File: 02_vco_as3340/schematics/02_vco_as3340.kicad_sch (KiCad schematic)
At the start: 89 parts, among them J1 Header 1, J10 SINE OUT, J2 Header 2, J3 SYNC IN, J4 FM IN, J5 PWM CV IN, J6 1V per O IN, J7 SQUARE OUT, J8 SAW OUT, J9 TRI OUT, Q1 BC547C, Q2 BC547C, U1 TL072, U2 AS3340, U3 TL074

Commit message: routed everyting
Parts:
- removed J1: Header 1, Connector_PinHeader_2.54mm:PinHeader_1x09_P2.54mm_Vertical, symbol Connector:Conn_01x09_Pin
- removed J2: Header 2, Connector_PinHeader_2.54mm:PinHeader_1x09_P2.54mm_Vertical, symbol Connector:Conn_01x09_Pin
- added J11: Header 1, Connector_PinSocket_2.54mm:PinSocket_2x05_P2.54mm_Vertical, symbol Connector_Generic:Conn_02x05_Counter_Clockwise
- added J12: Header 2, Connector_PinSocket_2.54mm:PinSocket_2x04_P2.54mm_Vertical, symbol Connector_Generic:Conn_02x04_Counter_Clockwise
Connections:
- net +12V: now also J11.3 (Pin_3)
- net -12V: now also J11.5 (Pin_5)
- net Coarse Tuning: now also J11.2 (Pin_2)
- net FM CV Hot: now also J12.4 (Pin_4)
- net FM CV Levelled: now also J11.1 (Pin_1)
- net Fine Tuning: now also J12.5 (Pin_5)
- net GND: now also J11.4 (Pin_4)
- net Hard Sync: now also J11.9 (Pin_9)
- net Hard Sync +: now also J11.10 (Pin_10)
- net Hard Sync -: now also J11.8 (Pin_8)
- net Mode COM: now also J12.6 (Pin_6)
- net Mode LFO: now also J12.8 (Pin_8)
- net Mode VCO: now also J12.7 (Pin_7)
- net PWM CV Hot: now also J12.2 (Pin_2)
- net PWM CV Levelled: now also J12.3 (Pin_3)
- net PWM Offset: now also J11.6 (Pin_6)
- net Soft Sync: now also J11.7 (Pin_7)
- net Sync COM: now also J12.1 (Pin_1)

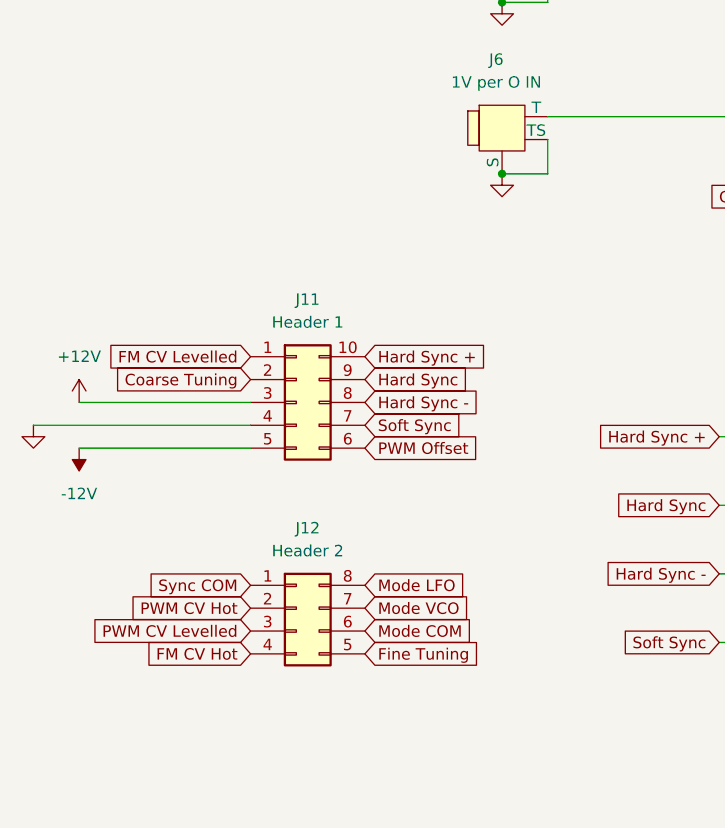
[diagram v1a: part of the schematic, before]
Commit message: fixed layout front/back
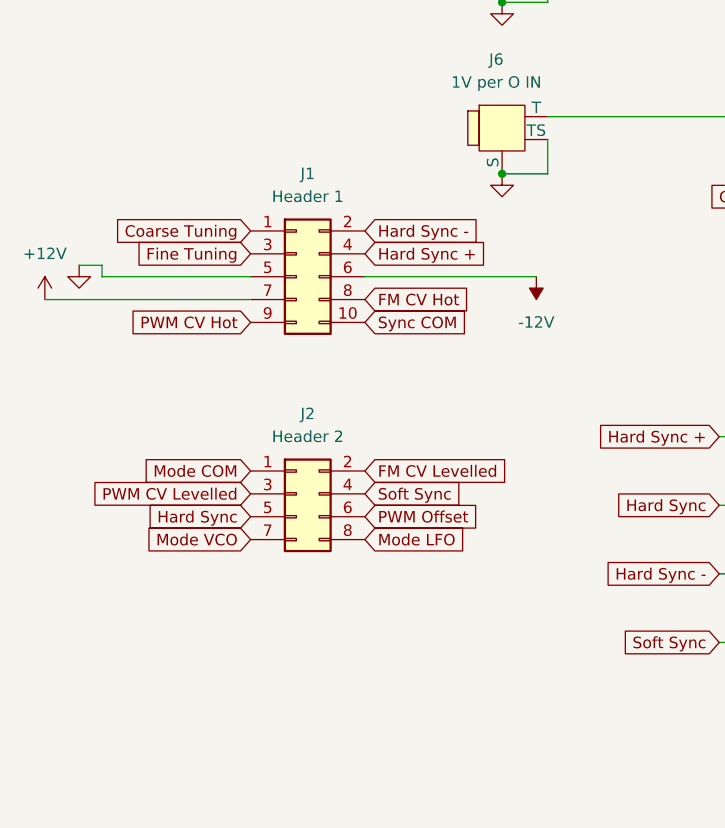
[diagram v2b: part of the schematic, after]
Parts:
- removed J11: Header 1, Connector_PinSocket_2.54mm:PinSocket_2x05_P2.54mm_Vertical, symbol Connector_Generic:Conn_02x05_Counter_Clockwise
- removed J12: Header 2, Connector_PinSocket_2.54mm:PinSocket_2x04_P2.54mm_Vertical, symbol Connector_Generic:Conn_02x04_Counter_Clockwise
- added J1: Header 1, Connector_PinSocket_2.54mm:PinSocket_2x05_P2.54mm_Vertical, symbol Connector_Generic:Conn_02x05_Odd_Even
- added J2: Header 2, Connector_PinSocket_2.54mm:PinSocket_2x04_P2.54mm_Vertical, symbol Connector_Generic:Conn_02x04_Odd_Even
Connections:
- net +12V: now also J1.7 (Pin_7)
- net -12V: now also J1.6 (Pin_6)
- net Coarse Tuning: now also J1.1 (Pin_1)
- net FM CV Hot: now also J1.8 (Pin_8)
- net FM CV Levelled: now also J2.2 (Pin_2)
- net Fine Tuning: now also J1.3 (Pin_3)
- net GND: now also J1.5 (Pin_5)
- net Hard Sync: now also J2.5 (Pin_5)
- net Hard Sync +: now also J1.4 (Pin_4)
- net Hard Sync -: now also J1.2 (Pin_2)
- net Mode COM: now also J2.1 (Pin_1)
- net Mode LFO: now also J2.8 (Pin_8)
- net Mode VCO: now also J2.7 (Pin_7)
- net PWM CV Hot: now also J1.9 (Pin_9)
- net PWM CV Levelled: now also J2.3 (Pin_3)
- net PWM Offset: now also J2.6 (Pin_6)
- net Soft Sync: now also J2.4 (Pin_4)
- net Sync COM: now also J1.10 (Pin_10)

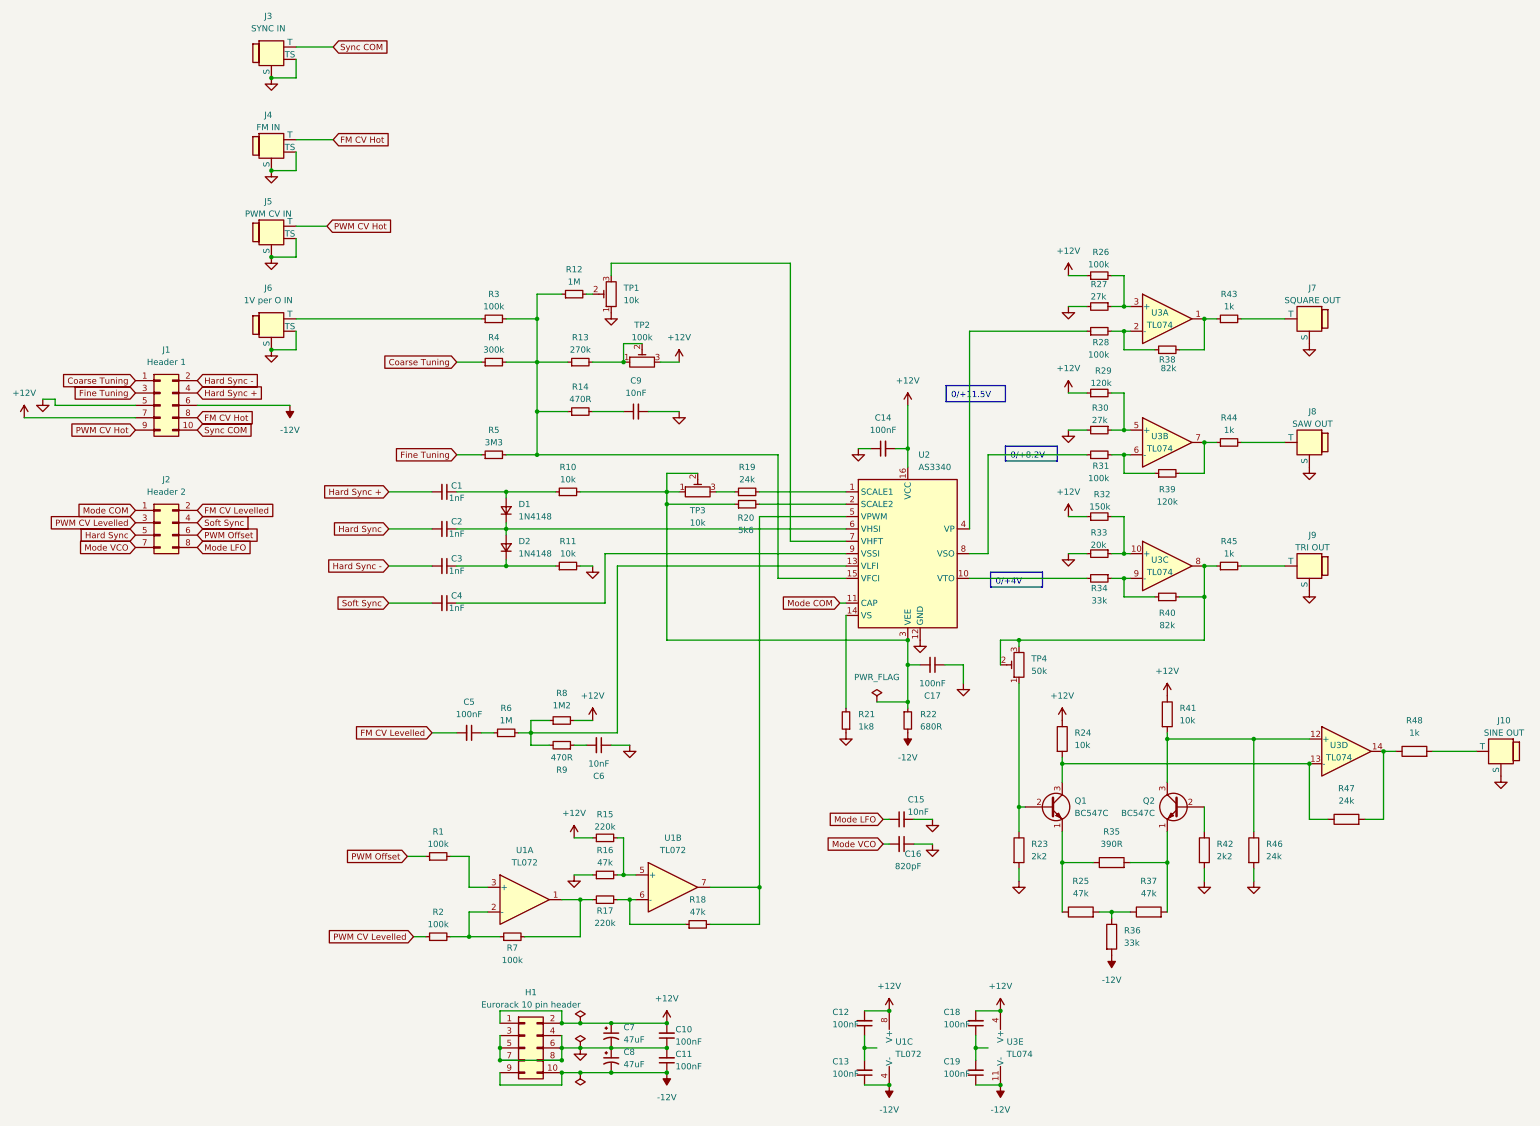
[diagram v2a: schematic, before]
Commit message: fine-tuned PCB hole distanes
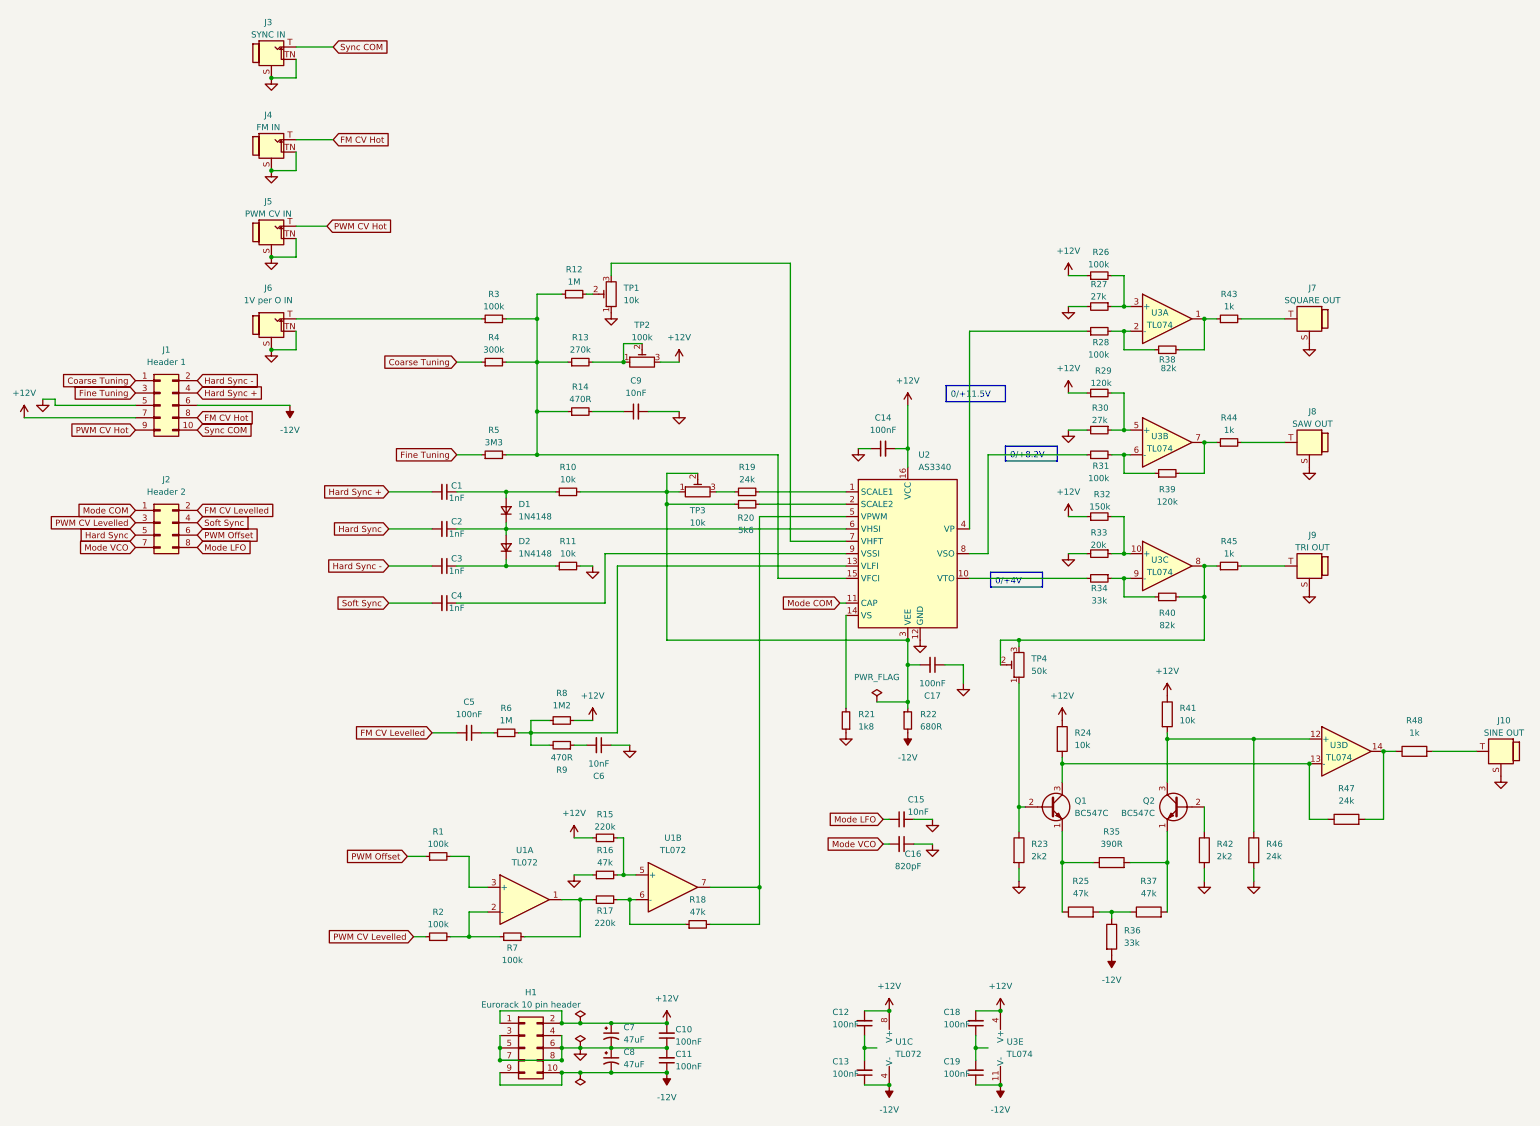
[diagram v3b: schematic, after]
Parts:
- J10, J7, J8, J9: footprint cynthia:6.35 mm jack socket mono -> cynthia:6.35 mm jack socket mono in 3 pin socket tip pin west
- J3, J4, J5, J6: footprint cynthia:6.35 mm jack socket mono switched -> cynthia:6.35 mm jack socket mono switched in 5 pin socket
- U1: footprint Package_DIP:DIP-8_W7.62mm -> Package_DIP:DIP-8_W7.62mm_Socket
- U2: footprint Package_DIP:DIP-16_W7.62mm -> Package_DIP:DIP-16_W7.62mm_Socket
- U3: footprint Package_DIP:DIP-14_W7.62mm -> Package_DIP:DIP-14_W7.62mm_Socket
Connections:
- net FM CV Hot: now also J4.T; no longer J4.1 (T)
- net GND: now also J10.S, J3.S, J3.TN, J4.S, J4.TN, J5.S, J5.TN, J6.S, J6.TN, J7.S, J8.S, J9.S; no longer J10.2 (S), J3.2 (TS), J3.3 (S), J4.2 (TS), J4.3 (S), J5.2 (TS), J5.3 (S), J6.2 (TS), J6.3 (S), J7.2 (S), J8.2 (S), J9.2 (S)
- net PWM CV Hot: now also J5.T; no longer J5.1 (T)
- net Sync COM: now also J3.T; no longer J3.1 (T)
- net at R3.1: now also J6.T; no longer J6.1 (T)
- net at R44.2: now also J8.T; no longer J8.1 (T)
- net at R43.2: now also J7.T; no longer J7.1 (T)
- net at R45.2: now also J9.T; no longer J9.1 (T)
- net at R48.2: now also J10.T; no longer J10.1 (T)

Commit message: final tweaks
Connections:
- net GND: now also C12.1, C13.2, C18.1, C19.2
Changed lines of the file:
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@@
 	)
 	(symbol
+		(lib_id "power:GND")
+		(at 227.33 261.62 0)
+		(unit 1)
+		(exclude_from_sim no)
+		(in_bom yes)
+		(on_board yes)
+		(dnp no)
+		(fields_autoplaced yes)
+		(property "Reference" "#PWR049"
+			(at 227.33 267.97 0)
+			(effects
+				(font
+					(size 1.27 1.27)
+				)
+				(hide yes)
+			)
+		)
+		(property "Value" "GND"
+			(at 227.33 266.7 0)
+			(effects
+				(font
+					(size 1.27 1.27)
+				)
+				(hide yes)
+			)
+		)
+		(property "Footprint" ""
+			(at 227.33 261.62 0)
+			(effects
+				(font
+					(size 1.27 1.27)
+				)
+				(hide yes)
+			)
+		)
+		(property "Datasheet" ""
+			(at 227.33 261.62 0)
+			(effects
+				(font
+					(size 1.27 1.27)
+				)
+				(hide yes)
+			)
+		)
+		(property "Description" "Power symbol creates a global label with name \"GND\" , ground"
+			(at 227.33 261.62 0)
+			(effects
+				(font
+					(size 1.27 1.27)
+				)
+				(hide yes)
+			)
+		)
+		(pin "1"
+		)
+		(instances
+			(project "02_vco_as3340"
+				(path "/7bf3d2ed-8bab-4c92-b1a7-3c419691fd96"
+					(reference "#PWR049")
+					(unit 1)
+				)
+			)
+		)
+	)
+	(symbol
 		(lib_id "Amplifier_Operational:TL074")
 		(at 264.16 162.56 0)
@@
 					(unit 1)
 				)
+			)
+		)
+	)
+	(symbol
+		(lib_id "power:GND")
+		(at 204.47 261.62 0)
+		(unit 1)
+		(exclude_from_sim no)
+		(in_bom yes)
+		(on_board yes)
+		(dnp no)
+		(fields_autoplaced yes)
+		(property "Reference" "#PWR048"
+			(at 204.47 267.97 0)
+			(effects
+				(font
+					(size 1.27 1.27)
+				)
+				(hide yes)
+			)
+		)
+		(property "Value" "GND"
+			(at 204.47 266.7 0)
+			(effects
+				(font
+					(size 1.27 1.27)
+				)
+				(hide yes)
+			)
+		)
+		(property "Footprint" ""
+			(at 204.47 261.62 0)
+			(effects
+				(font
+					(size 1.27 1.27)
+				)
+				(hide yes)
+			)
+		)
+		(property "Datasheet" ""
+			(at 204.47 261.62 0)
+			(effects
+				(font
+					(size 1.27 1.27)
+				)
+				(hide yes)
+			)
+		)
+		(property "Description" "Power symbol creates a global label with name \"GND\" , ground"
+			(at 204.47 261.62 0)
+			(effects
+				(font
+					(size 1.27 1.27)
+				)
+				(hide yes)
+			)
+		)
+		(pin "1"
+		)
+		(instances
+			(project "02_vco_as3340"
+				(path "/7bf3d2ed-8bab-4c92-b1a7-3c419691fd96"
+					(reference "#PWR048")
+					(unit 1)
+				)
